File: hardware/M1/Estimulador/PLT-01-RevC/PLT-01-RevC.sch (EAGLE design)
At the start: 57 parts, among them T1 2N2222, T2 2N2222, T3 2N2222, T4 2N2222, T5 2N2222, T6 2N2222

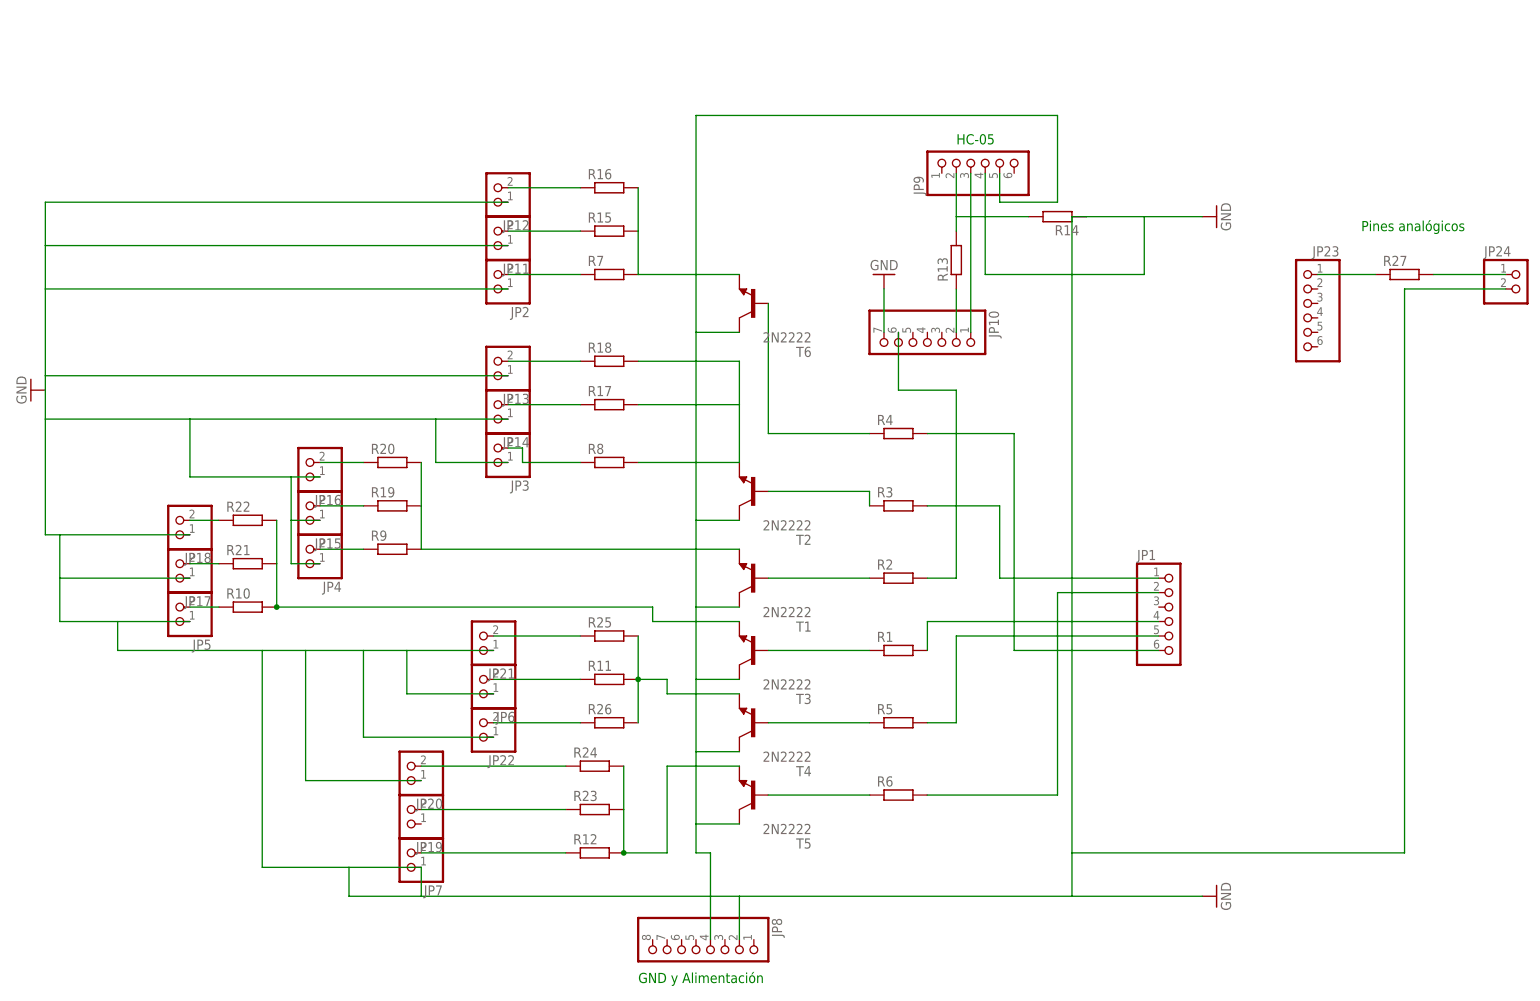
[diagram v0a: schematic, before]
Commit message: Se sube RevC de placa M1
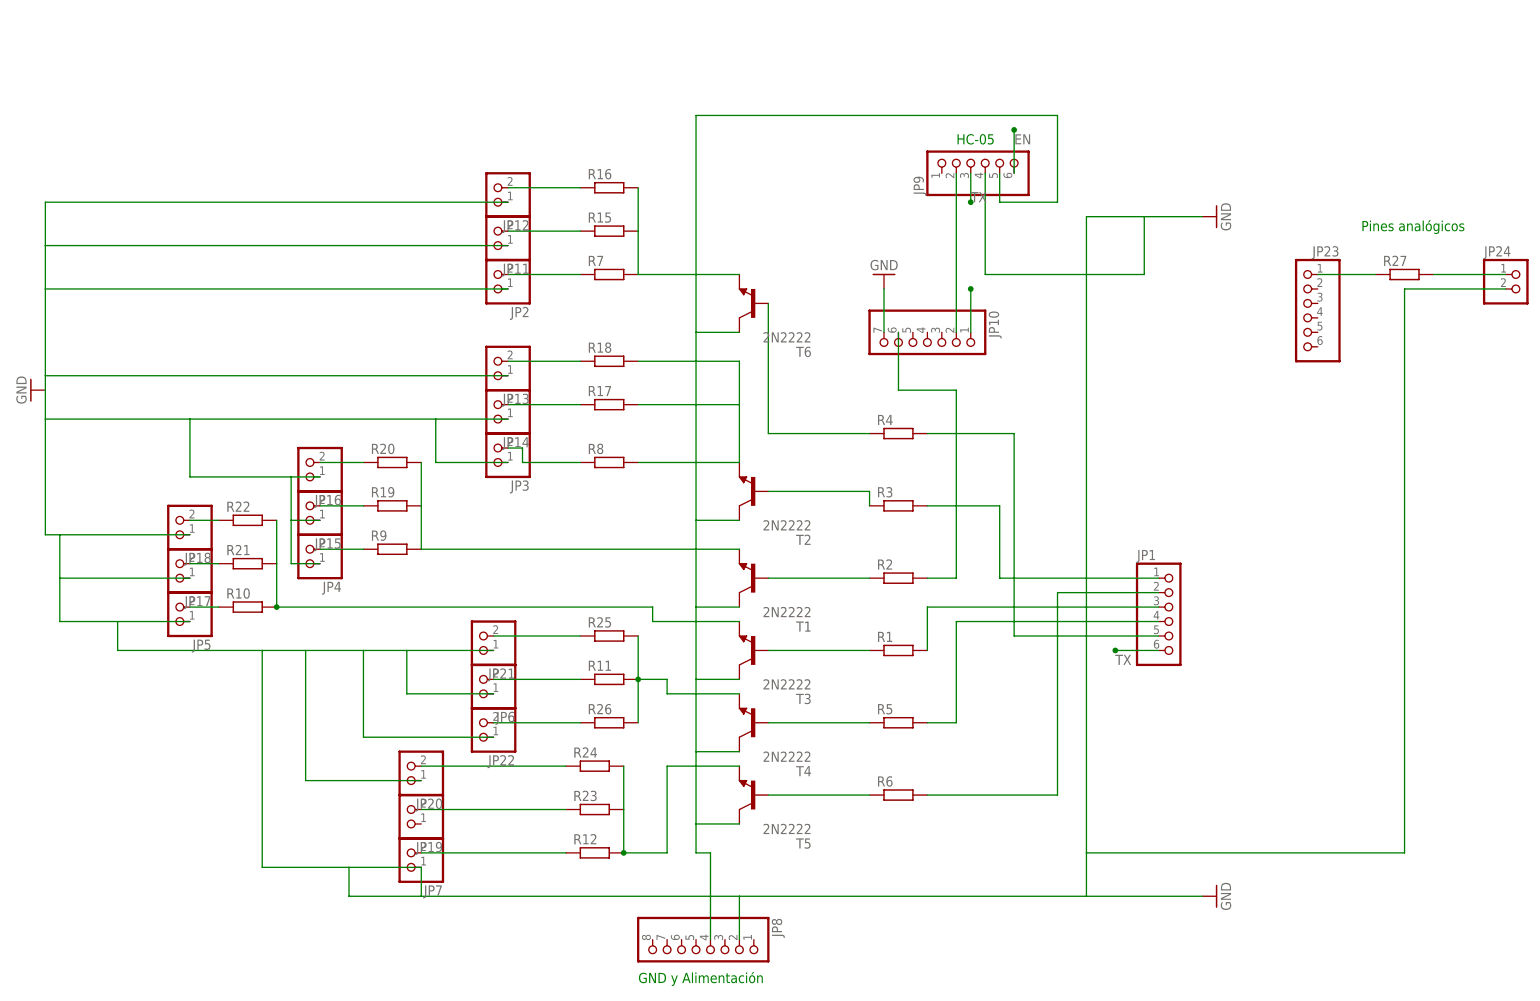
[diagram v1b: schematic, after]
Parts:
- removed R13, R14: (no value), resistor:R-EU_0207/10
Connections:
- removed net N$26: JP9.2, R13.2, R14.2
- removed net N$27: JP10.1, JP9.3
- new net EN: JP10.1, JP9.6
- new net TX: JP1.6, JP9.3
- net GND: no longer R14.1
- net N$1: now also JP1.5; no longer JP1.6
- net N$25: now also JP9.2; no longer R13.1
- net N$4: now also JP1.3; no longer JP1.4
- net N$5: now also JP1.4; no longer JP1.5
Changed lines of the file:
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@@
 <part name="JP9" library="pinhead" deviceset="PINHD-1X6" device=""/>
 <part name="JP10" library="pinhead" deviceset="PINHD-1X7" device=""/>
-<part name="R13" library="resistor" deviceset="R-EU_" device="0207/10"/>
-<part name="R14" library="resistor" deviceset="R-EU_" device="0207/10"/>
 <part name="JP11" library="pinhead" deviceset="PINHD-1X2" device=""/>
 <part name="R15" library="resistor" deviceset="R-EU_" device="0207/10"/>
@@
 <instance part="JP9" gate="A" x="73.66" y="101.6" rot="R90"/>
 <instance part="JP10" gate="A" x="63.5" y="68.58" rot="R270"/>
-<instance part="R13" gate="G$1" x="68.58" y="83.82" rot="R90"/>
-<instance part="R14" gate="G$1" x="86.36" y="91.44" rot="R180"/>
 <instance part="JP11" gate="G$1" x="-12.7" y="88.9" rot="R180"/>
 <instance part="R15" gate="G$1" x="7.62" y="88.9"/>
@@
 <pinref part="R4" gate="G$1" pin="2"/>
 <wire x1="78.74" y1="53.34" x2="63.5" y2="53.34" width="0.1524" layer="91"/>
-<wire x1="78.74" y1="15.24" x2="78.74" y2="53.34" width="0.1524" layer="91"/>
-<pinref part="JP1" gate="A" pin="6"/>
-<wire x1="78.74" y1="15.24" x2="104.14" y2="15.24" width="0.1524" layer="91"/>
+<wire x1="78.74" y1="17.78" x2="78.74" y2="53.34" width="0.1524" layer="91"/>
+<pinref part="JP1" gate="A" pin="5"/>
+<wire x1="104.14" y1="17.78" x2="78.74" y2="17.78" width="0.1524" layer="91"/>
 </segment>
 </net>
@@
 <net name="N$4" class="0">
 <segment>
-<pinref part="JP1" gate="A" pin="4"/>
 <pinref part="R1" gate="G$1" pin="2"/>
-<wire x1="104.14" y1="20.32" x2="63.5" y2="20.32" width="0.1524" layer="91"/>
-<wire x1="63.5" y1="20.32" x2="63.5" y2="15.24" width="0.1524" layer="91"/>
+<wire x1="63.5" y1="22.86" x2="63.5" y2="15.24" width="0.1524" layer="91"/>
+<pinref part="JP1" gate="A" pin="3"/>
+<wire x1="104.14" y1="22.86" x2="63.5" y2="22.86" width="0.1524" layer="91"/>
 </segment>
 </net>
 <net name="N$5" class="0">
 <segment>
-<pinref part="JP1" gate="A" pin="5"/>
-<wire x1="104.14" y1="17.78" x2="68.58" y2="17.78" width="0.1524" layer="91"/>
-<wire x1="68.58" y1="17.78" x2="68.58" y2="2.54" width="0.1524" layer="91"/>
+<wire x1="68.58" y1="20.32" x2="68.58" y2="2.54" width="0.1524" layer="91"/>
 <pinref part="R5" gate="G$1" pin="2"/>
 <wire x1="68.58" y1="2.54" x2="63.5" y2="2.54" width="0.1524" layer="91"/>
+<pinref part="JP1" gate="A" pin="4"/>
+<wire x1="104.14" y1="20.32" x2="68.58" y2="20.32" width="0.1524" layer="91"/>
 </segment>
 </net>
@@
 <segment>
 <pinref part="JP10" gate="A" pin="2"/>
-<pinref part="R13" gate="G$1" pin="1"/>
-<wire x1="68.58" y1="71.12" x2="68.58" y2="78.74" width="0.1524" layer="91"/>
-</segment>
-</net>
-<net name="N$26" class="0">
-<segment>
-<pinref part="R13" gate="G$1" pin="2"/>
 <pinref part="JP9" gate="A" pin="2"/>
-<wire x1="68.58" y1="88.9" x2="68.58" y2="91.44" width="0.1524" layer="91"/>
-<pinref part="R14" gate="G$1" pin="2"/>
-<wire x1="68.58" y1="91.44" x2="68.58" y2="99.06" width="0.1524" layer="91"/>
-<wire x1="68.58" y1="91.44" x2="81.28" y2="91.44" width="0.1524" layer="91"/>
-</segment>
-</net>
-<net name="N$27" class="0">
-<segment>
-<pinref part="JP10" gate="A" pin="1"/>
-<pinref part="JP9" gate="A" pin="3"/>
-<wire x1="71.12" y1="71.12" x2="71.12" y2="99.06" width="0.1524" layer="91"/>
+<wire x1="68.58" y1="71.12" x2="68.58" y2="99.06" width="0.1524" layer="91"/>
 </segment>
 </net>
 <net name="GND" class="0">
 <segment>
-<pinref part="R14" gate="G$1" pin="1"/>
 <wire x1="91.44" y1="91.44" x2="101.6" y2="91.44" width="0.1524" layer="91"/>
 <pinref part="JP9" gate="A" pin="4"/>
 <wire x1="73.66" y1="81.28" x2="73.66" y2="99.06" width="0.1524" layer="91"/>
-<wire x1="73.66" y1="81.28" x2="101.6" y2="81.28" width="0.1524" layer="91"/>
+<wire x1="73.66" y1="81.28" x2="91.44" y2="81.28" width="0.1524" layer="91"/>
+<wire x1="91.44" y1="81.28" x2="101.6" y2="81.28" width="0.1524" layer="91"/>
 <wire x1="101.6" y1="81.28" x2="101.6" y2="91.44" width="0.1524" layer="91"/>
 <wire x1="101.6" y1="91.44" x2="111.76" y2="91.44" width="0.1524" layer="91"/>
 <pinref part="JP8" gate="A" pin="2"/>
 <wire x1="30.48" y1="-27.94" x2="30.48" y2="-35.56" width="0.1524" layer="91"/>
-<wire x1="111.76" y1="-27.94" x2="88.9" y2="-27.94" width="0.1524" layer="91"/>
-<wire x1="88.9" y1="-27.94" x2="30.48" y2="-27.94" width="0.1524" layer="91"/>
-<wire x1="91.44" y1="91.44" x2="88.9" y2="91.44" width="0.1524" layer="91"/>
-<wire x1="88.9" y1="91.44" x2="88.9" y2="-20.32" width="0.1524" layer="91"/>
+<wire x1="111.76" y1="-27.94" x2="91.44" y2="-27.94" width="0.1524" layer="91"/>
+<wire x1="91.44" y1="-27.94" x2="30.48" y2="-27.94" width="0.1524" layer="91"/>
+<wire x1="91.44" y1="91.44" x2="91.44" y2="81.28" width="0.1524" layer="91"/>
+<wire x1="91.44" y1="81.28" x2="91.44" y2="-20.32" width="0.1524" layer="91"/>
 <pinref part="GND2" gate="1" pin="GND"/>
 <pinref part="JP24" gate="G$1" pin="2"/>
-<wire x1="88.9" y1="-20.32" x2="88.9" y2="-27.94" width="0.1524" layer="91"/>
+<wire x1="91.44" y1="-20.32" x2="91.44" y2="-27.94" width="0.1524" layer="91"/>
 <wire x1="165.1" y1="78.74" x2="147.32" y2="78.74" width="0.1524" layer="91"/>
 <wire x1="147.32" y1="78.74" x2="147.32" y2="-20.32" width="0.1524" layer="91"/>
-<wire x1="147.32" y1="-20.32" x2="88.9" y2="-20.32" width="0.1524" layer="91"/>
+<wire x1="147.32" y1="-20.32" x2="91.44" y2="-20.32" width="0.1524" layer="91"/>
 <pinref part="JP12" gate="G$1" pin="1"/>
 <pinref part="GND1" gate="1" pin="GND"/>
@@
 </segment>
 </net>
+<net name="TX" class="0">
+<segment>
+<pinref part="JP9" gate="A" pin="3"/>
+<wire x1="71.12" y1="99.06" x2="71.12" y2="93.98" width="0.1524" layer="91"/>
+<junction x="71.12" y="93.98"/>
+<label x="71.12" y="93.98" size="1.778" layer="95"/>
+</segment>
+<segment>
+<pinref part="JP1" gate="A" pin="6"/>
+<wire x1="104.14" y1="15.24" x2="96.52" y2="15.24" width="0.1524" layer="91"/>
+<junction x="96.52" y="15.24"/>
+<label x="96.52" y="12.7" size="1.778" layer="95"/>
+</segment>
+</net>
+<net name="EN" class="0">
+<segment>
+<pinref part="JP9" gate="A" pin="6"/>
+<wire x1="78.74" y1="99.06" x2="78.74" y2="106.68" width="0.1524" layer="91"/>
+<junction x="78.74" y="106.68"/>
+<label x="78.74" y="104.14" size="1.778" layer="95"/>
+</segment>
+<segment>
+<pinref part="JP10" gate="A" pin="1"/>
+<wire x1="71.12" y1="71.12" x2="71.12" y2="78.74" width="0.1524" layer="91"/>
+<junction x="71.12" y="78.74"/>
+</segment>
+</net>

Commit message: Se corrige plaga RevC
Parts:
- added JP25: (no value), pinhead:PINHD-1X2
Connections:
- removed net EN: JP10.1, JP9.6
- new net N$6: JP25.1, JP9.6
- net 5V: now also JP25.2
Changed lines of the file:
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@@
 <part name="GND3" library="supply1" deviceset="GND" device=""/>
 <part name="GND4" library="supply1" deviceset="GND" device=""/>
+<part name="JP25" library="pinhead" deviceset="PINHD-1X2" device=""/>
 </parts>
 <sheets>
@@
 <instance part="GND3" gate="1" x="55.88" y="81.28" rot="R180"/>
 <instance part="GND4" gate="1" x="114.3" y="91.44" rot="R90"/>
+<instance part="JP25" gate="G$1" x="76.2" y="121.92" rot="R180"/>
 </instances>
 <busses>
@@
 <pinref part="T6" gate="G$1" pin="C"/>
 <wire x1="30.48" y1="71.12" x2="22.86" y2="71.12" width="0.1524" layer="91"/>
+</segment>
+<segment>
+<pinref part="JP25" gate="G$1" pin="2"/>
+<wire x1="78.74" y1="121.92" x2="78.74" y2="127" width="0.1524" layer="91"/>
+<junction x="78.74" y="127"/>
 </segment>
 </net>
@@
 </segment>
 </net>
-<net name="EN" class="0">
+<net name="N$6" class="0">
 <segment>
 <pinref part="JP9" gate="A" pin="6"/>
-<wire x1="78.74" y1="99.06" x2="78.74" y2="106.68" width="0.1524" layer="91"/>
-<junction x="78.74" y="106.68"/>
-<label x="78.74" y="104.14" size="1.778" layer="95"/>
-</segment>
-<segment>
-<pinref part="JP10" gate="A" pin="1"/>
-<wire x1="71.12" y1="71.12" x2="71.12" y2="78.74" width="0.1524" layer="91"/>
-<junction x="71.12" y="78.74"/>
-</segment>
-</net>
+<pinref part="JP25" gate="G$1" pin="1"/>
+<wire x1="78.74" y1="99.06" x2="78.74" y2="119.38" width="0.1524" layer="91"/>
+</segment>
+</net>
